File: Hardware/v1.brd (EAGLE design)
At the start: 77.5 x 32.6 mm, 23 parts, among them CN1 629105150521, CN2 TSW-120-08-L-S-RA, CN3 CONN_TE_DB9, CN4 CONN_TE_DB-HD15, IC1 ADUM3160BRWZ, IC3 IC_MAX3313, U1 TUSB2036VF

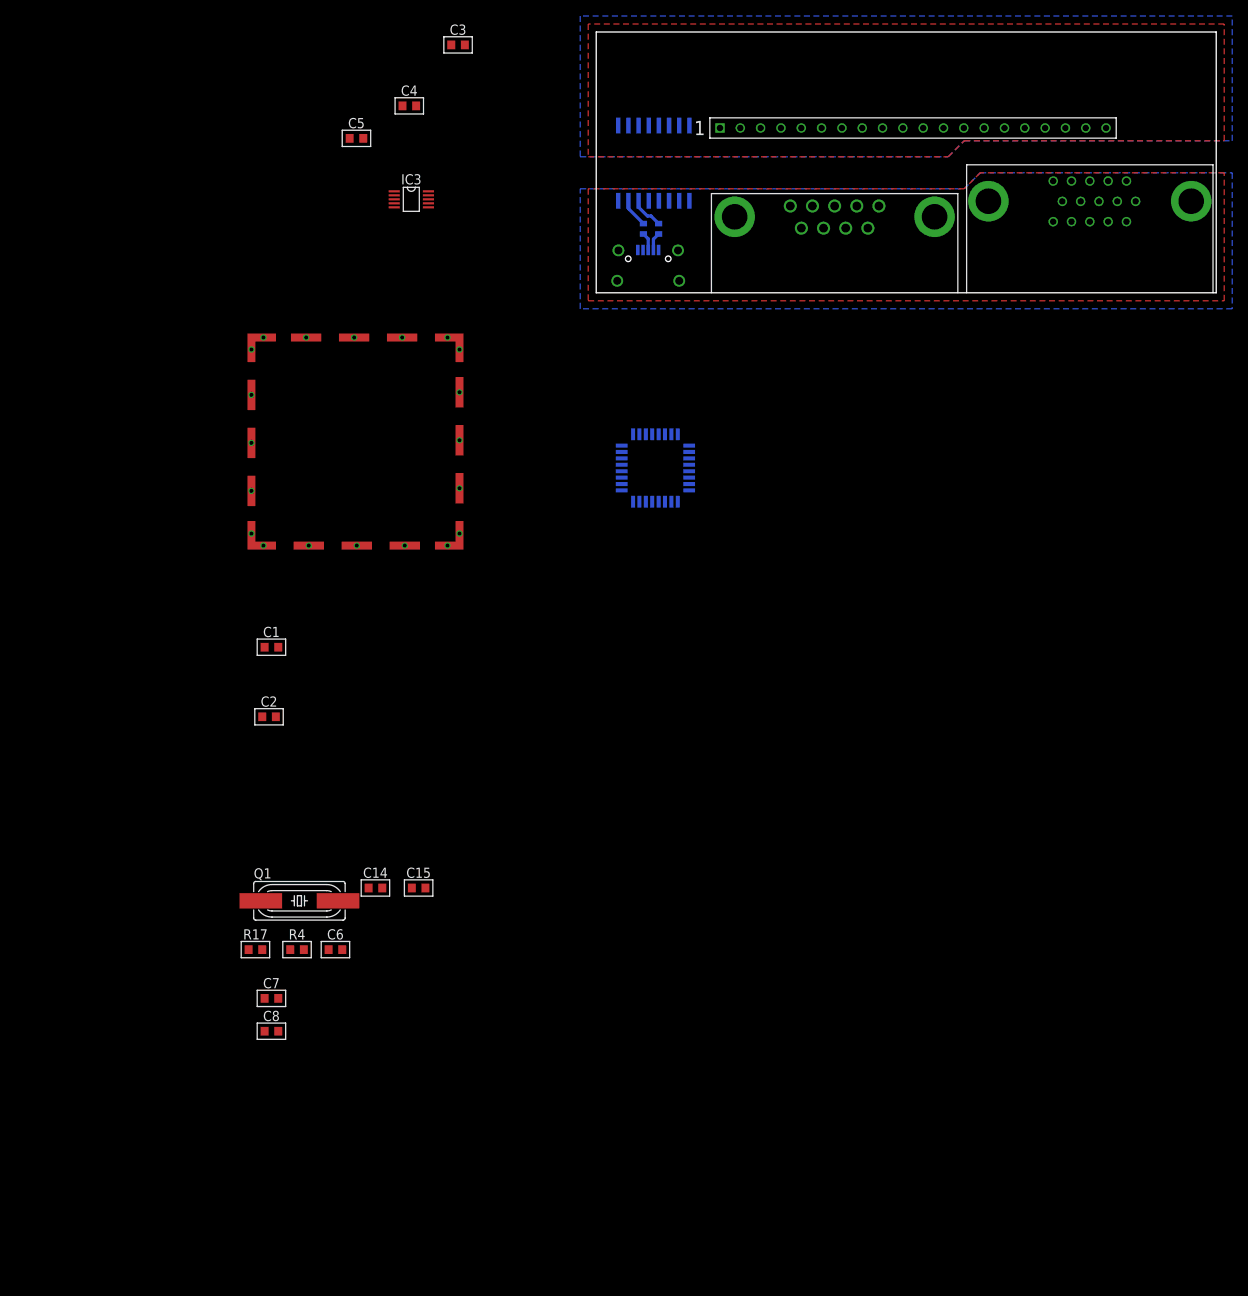
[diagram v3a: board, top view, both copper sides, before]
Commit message: finished input side of usb isolator
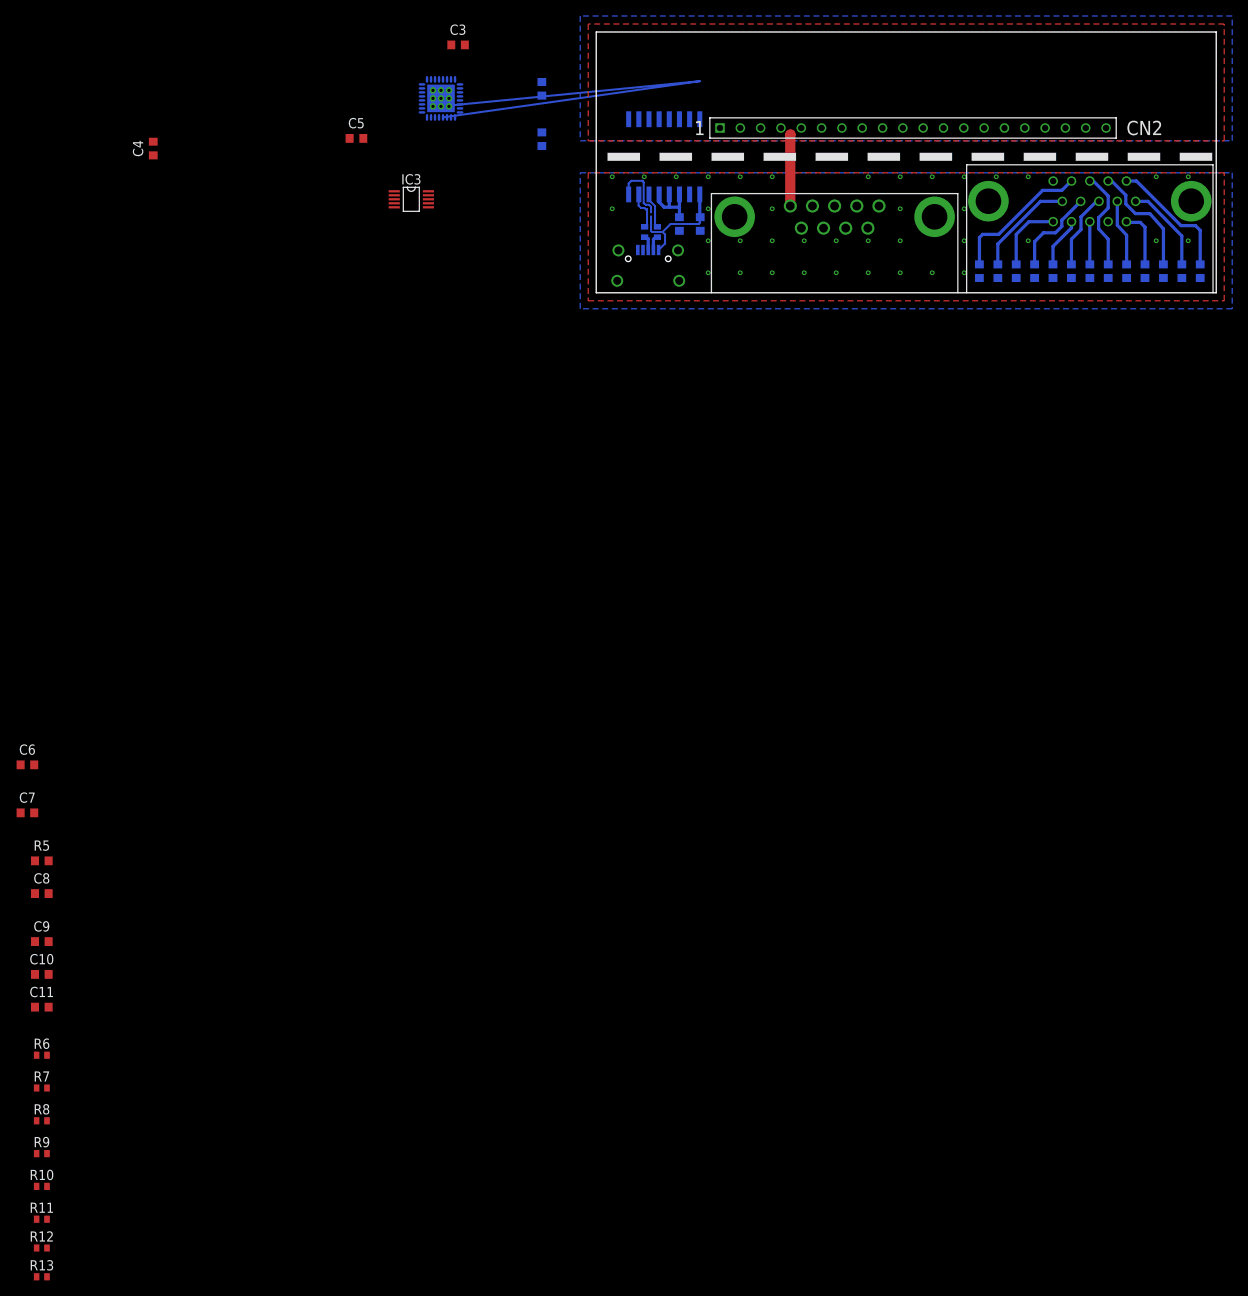
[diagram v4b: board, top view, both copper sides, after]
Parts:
- removed CAN1: CAN_LAIRD-BMI-S-203-F, m0wut:CAN_LAIRD_BMS-S-203-F
- removed Q1: (no value), adafruit:HC49UP
- removed R17: 1k5, rcl:R0603
- removed U1: TUSB2036VF, Texas Instruments_By_element14_Batch_1:QFP80P900X900X145-32N
- added C10, C11: 100nF, rcl:C0603
- added C12, C13, C16, C17, C18, C19, C20, C21, C22, C23, C24: 1nF, rcl:C0603
- added C9: 1uF, rcl:C0603
- added D1: D_ST_USBULC6, m0wut:UQFN6
- added IC2: TUSB2046BIRHBT, texas:RHB_S-PQFP-N32
- added R10, R11, R12, R13, R6, R7, R8, R9: 24, rcl:R0402
- added R3: 24, rcl:R0603
- added R5: 15k, rcl:R0603
- C14, C15: value 22pF -> 1nF
- CN3: value CONN_TE_DB9 -> 1734354-1
- CN4: value CONN_TE_DB-HD15 -> 1-1734530-1
- R4: value 15k -> 24
- moved C14 119.7 mm to (64.0, 2.70), flipped to the bottom, turned to 270 degrees
- moved R4 111.9 mm to (-6.80, 25.5), flipped to the bottom, turned to 90 degrees
- moved C15 104.2 mm to (47.9, 2.70), flipped to the bottom, turned to 270 degrees
- moved C2 80.2 mm to (10.4, 8.60), flipped to the bottom, turned to 270 degrees
- moved C1 75.3 mm to (13.0, 8.60), flipped to the bottom, turned to 270 degrees
- moved C6 44.9 mm to (-71.1, -59.0)
- moved C7 38.3 mm to (-71.1, -65.0)
- moved C8 33.5 mm to (-69.3, -75.1)
- moved C4 32.4 mm to (-55.4, 18.0), turned to 90 degrees
- moved IC1 1.53 mm to (8.50, 17.0)
- moved R1 0.43 mm to (6.05, 7.60)
- moved R2 0.43 mm to (7.65, 7.60)
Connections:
- removed net DP0PUR: U1.27
- removed net XTAL1: C14.1, Q1.1, U1.30
- removed net XTAL2: R17.2, U1.29
- new net 6MHZ_HUB: IC2.30
- new net D+: D1.1, D1.6, IC1.7, R1.2
- new net D-: D1.3, D1.4, IC1.6, R2.2
- new net DM4: R7.2
- new net DP4: R6.2
- new net N$12: IC2.11, R8.2
- new net N$13: IC2.12, R9.2
- new net N$14: IC2.15, R10.2
- new net N$15: IC2.16, R11.2
- new net N$16: IC2.20, R12.1
- new net N$17: IC2.19, R13.1
- new net N$18: C23.1, CN4.14
- new net N$19: CN4.12
- new net N$20: CN4.5
- new net N$21: C24.1, CN4.15
- new net N$22: C22.1, CN4.13
- new net N$23: C21.1, CN4.11
- new net N$24: C20.1, CN4.10
- new net N$25: C19.1, CN4.9
- new net N$26: C18.1, CN4.8
- new net N$27: C17.1, CN4.7
- new net N$28: C16.1, CN4.6
- new net N$29: C15.1, CN4.4
- new net N$30: C14.1, CN4.3
- new net N$31: C13.1, CN4.2
- new net N$32: C12.1, CN4.1
- new net VCC: C1.1, CN1.1, D1.5, IC1.1
- net +3V3: now also C10.1, C11.1, C6.1, C9.1, IC2.25, IC2.26, IC2.3, R5.1; no longer C8.1, R4.1, U1.10, U1.14, U1.18, U1.24, U1.25, U1.26, U1.3, U1.8
- net AGND: now also C12.2, C13.2, C14.2, C15.2, C16.2, C17.2, C18.2, C19.2, C20.2, C21.2, C22.2, C23.2, C24.2, CN3.TAB, CN3.TAB1, CN4.16, CN4.17, D1.2
- net DM0: now also IC2.2, R3.2; no longer IC1.11, U1.2
- net DM1: now also R8.1; no longer U1.11
- net DM2: now also R10.1; no longer U1.15
- net DM3: now also R13.2; no longer U1.19
- net DP0: now also IC2.1, R4.2; no longer IC1.10, U1.1
- net DP1: now also R9.1; no longer U1.12
- net DP2: now also R11.1; no longer U1.16
- net DP3: now also R12.2; no longer U1.20
- net GND: now also C10.2, C11.2, C6.2, C9.2, CN3.5, IC2.27, IC2.28, IC2.31, IC2.6, IC2.7, IC2.8, IC2.EXP, IC2.EXP@1, IC2.EXP@2, IC2.EXP@3, IC2.EXP@4, IC2.EXP@5, IC2.EXP@6, IC2.EXP@7, IC2.EXP@8, IC2.EXP@9; no longer C14.2, C15.2, C6.1, CAN1.P$1, CAN1.P$10, CAN1.P$11, CAN1.P$12, CAN1.P$13, CAN1.P$14, CAN1.P$15, CAN1.P$16, CAN1.P$17, CAN1.P$18, CAN1.P$19, CAN1.P$2, CAN1.P$20, CAN1.P$21, CAN1.P$22, CAN1.P$23, CAN1.P$24, CAN1.P$25, CAN1.P$26, CAN1.P$27, CAN1.P$28, CAN1.P$29, CAN1.P$3, CAN1.P$30, CAN1.P$31, CAN1.P$32, CAN1.P$33, CAN1.P$34, CAN1.P$35, CAN1.P$36, CAN1.P$37, CAN1.P$38, CAN1.P$39, CAN1.P$4, CAN1.P$40, CAN1.P$5, CAN1.P$6, CAN1.P$7, CAN1.P$8, CAN1.P$9, U1.21, U1.22, U1.23, U1.28, U1.31, U1.6, U1.7
- net N$10: now also IC1.11, R3.1; no longer C6.2, R4.2, U1.4
- net N$11: now also IC1.10, R4.1; no longer C15.1, Q1.2, R17.1
- net N$3: now also C8.1, IC2.4, R5.2; no longer IC1.6, R2.2
- net N$4: now also IC2.24, R6.1; no longer IC1.7, R1.2
- net N$5: now also IC2.23, R7.1; no longer C1.1, CN1.1, IC1.1
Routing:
- net GND: track 0.00 -> 73.9 mm
- net N$29: track 0.00 -> 17.8 mm
- net N$32: track 0.00 -> 16.0 mm
- net VCC: track 0.00 -> 14.5 mm
- net N$31: track 0.00 -> 14.5 mm
- net N$24: track 0.00 -> 12.8 mm
- net N$30: track 0.00 -> 12.6 mm
- net N$28: track 0.00 -> 11.1 mm
- net N$25: track 0.00 -> 11.1 mm
- net N$26: track 0.00 -> 9.49 mm
- net N$21: track 0.00 -> 9.03 mm
- net N$27: track 0.00 -> 8.33 mm
- net N$9: track 0.00 -> 8.29 mm
- net AGND: track 0.00 -> 7.65 mm, vias 0 -> 39
- net N$23: track 0.00 -> 7.26 mm
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
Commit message: most of usb hub implemented
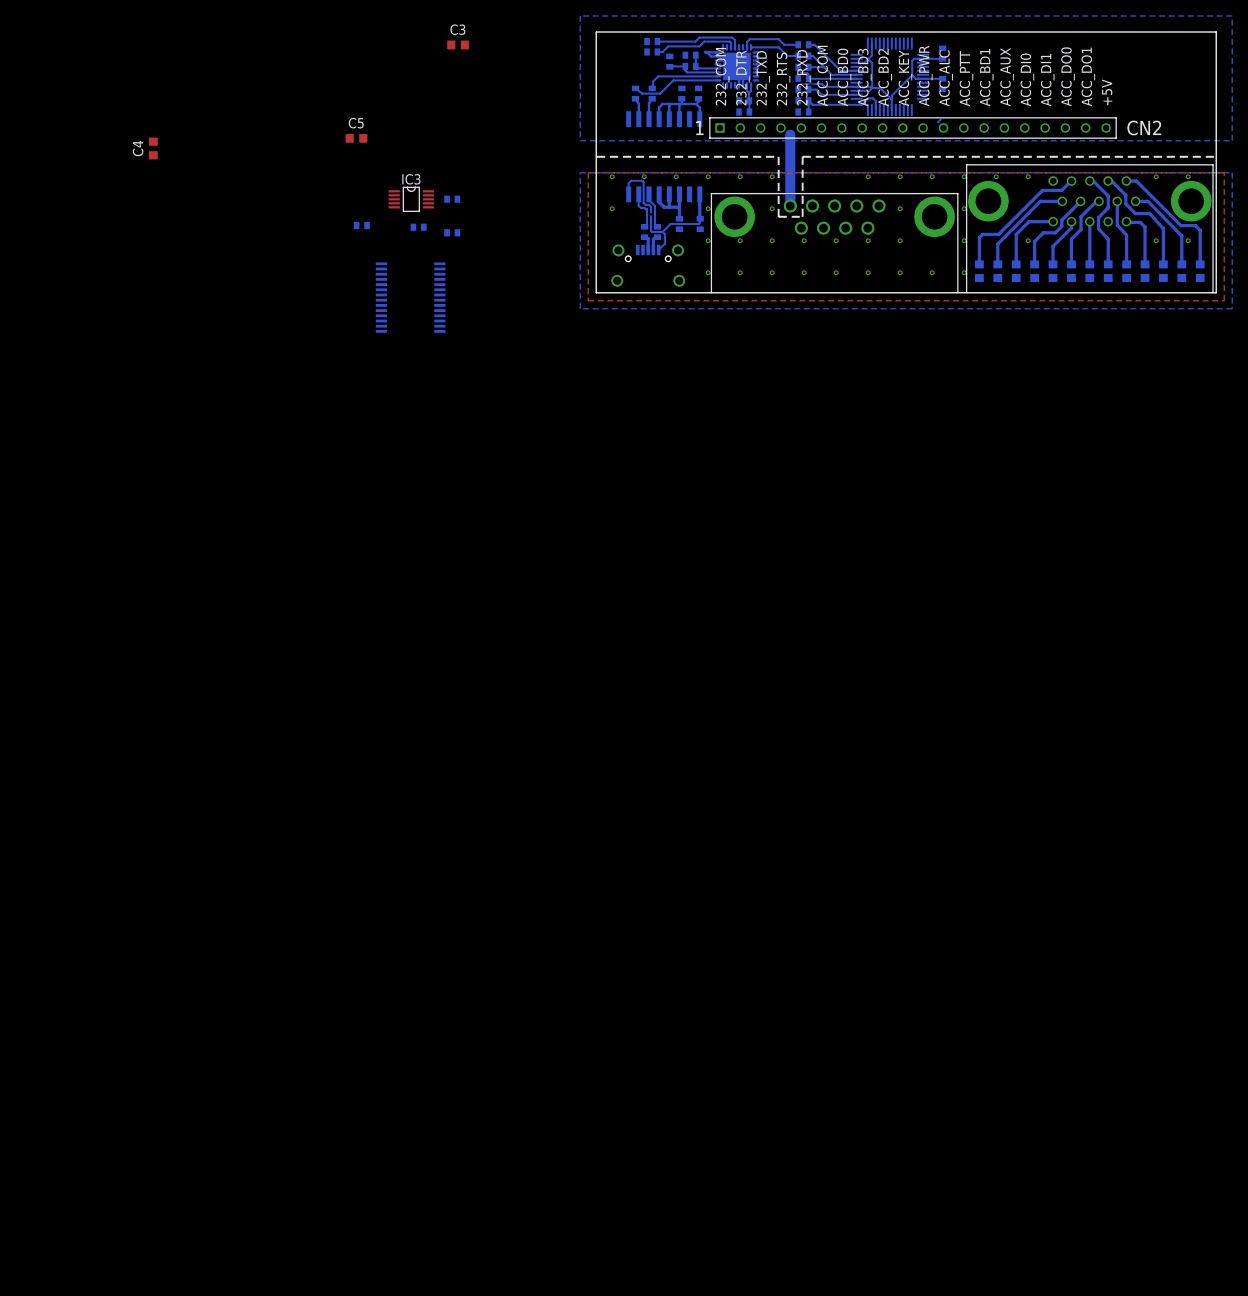
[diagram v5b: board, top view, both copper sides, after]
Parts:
- added C25, C27, C28: 100nF, rcl:C0402
- added C26: 33nF, rcl:C0402
- added IC4: FT2232D, ftdichip-3:QFP48-7X7
- added IC6: PCM2903C, texas:SSOP28DB
- added R14: 1k5, rcl:R0402
- added R15: 470, rcl:R0402
- added R16: 10k, rcl:R0402
- C1, C10, C11, C2, C6, C7, C8, C9: device rcl:C0603 -> rcl:C0402
- R3, R4, R5: device rcl:R0603 -> rcl:R0402
- moved R11 173.8 mm to (25.9, 29.6), flipped to the bottom
- moved R10 171.5 mm to (25.9, 31.0), flipped to the bottom
- moved R9 158.6 mm to (7.00, 31.4), flipped to the bottom, turned to 180 degrees
- moved R8 153.9 mm to (7.00, 30.1), flipped to the bottom, turned to 180 degrees
- moved R13 144.1 mm to (-18.0, 11.7), flipped to the bottom, turned to 180 degrees
- moved C11 141.9 mm to (9.20, 28.9), flipped to the bottom, turned to 90 degrees
- moved C10 140.1 mm to (18.5, 24.0), flipped to the bottom
- moved R12 136.9 mm to (-18.0, 7.50), flipped to the bottom, turned to 180 degrees
- moved C9 135.9 mm to (18.5, 22.6), flipped to the bottom
- moved C8 132.5 mm to (11.8, 29.7), flipped to the bottom
- moved R5 128.2 mm to (11.8, 28.3), flipped to the bottom, turned to 180 degrees
- moved C7 121.5 mm to (10.7, 24.9), flipped to the bottom, turned to 90 degrees
- moved C6 118.7 mm to (12.8, 24.9), flipped to the bottom, turned to 90 degrees
- moved R7 115.0 mm to (-29.3, 8.40), flipped to the bottom, turned to 180 degrees
- moved R6 113.7 mm to (-22.2, 8.20), flipped to the bottom, turned to 180 degrees
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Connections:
- new net 6MHZ_FT: IC4.43
- new net AGNDC: IC6.11
- new net AGNDP: IC6.18
- new net AGNDX: IC6.22
- new net CAT_232_TO_PIC: IC4.24
- new net CAT_PIC_TO_232: IC4.23
- new net DGND: IC6.26
- new net DGNDU: IC6.4
- new net N$33: C27.1, IC4.46, R15.1
- new net N$37: IC4.2, R16.2
- new net VBUS: IC6.3
- new net VCCCI: IC6.10
- new net VCCP2I: IC6.19
- new net VCCXI: IC6.23
- new net VCOM: IC6.14
- new net VDD: C26.1, IC4.6, R14.1
- new net VDDI: IC6.27
- new net WK_232_TO_PIC: IC4.40
- new net WK_PIC_TO_232: IC4.39
- net +5V: now also C25.1, C28.1, IC4.10, IC4.14, IC4.26, IC4.3, IC4.31, IC4.4, IC4.42, R15.2, R16.1
- net DM2: now also IC4.8
- net DM4: now also IC6.2
- net DP2: now also IC4.7, R14.2
- net DP4: now also IC6.1
- net GND: now also C25.2, C26.2, C27.2, C28.2, IC4.18, IC4.25, IC4.34, IC4.45, IC4.47, IC4.9; no longer IC2.EXP@1, IC2.EXP@2, IC2.EXP@3, IC2.EXP@4, IC2.EXP@5, IC2.EXP@6, IC2.EXP@7, IC2.EXP@8, IC2.EXP@9
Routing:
- net GND: track 73.9 -> 25.2 mm
- net +5V: track 0.00 -> 39.2 mm
- net +3V3: track 0.00 -> 24.8 mm
- net N$33: track 0.00 -> 11.6 mm
- net DP0: track 0.00 -> 11.2 mm
- net N$13: track 0.00 -> 10.9 mm
- net N$12: track 0.00 -> 10.4 mm
- net DM0: track 0.00 -> 9.26 mm
- net DP2: track 0.00 -> 8.92 mm
- net VDD: track 0.00 -> 8.43 mm
- net N$14: track 0.00 -> 7.51 mm
- net DM2: track 0.00 -> 7.35 mm
- net N$15: track 0.00 -> 6.35 mm
- net N$37: track 0.00 -> 6.27 mm
- net N$3: track 0.00 -> 4.28 mm
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- removed copper zone on layer 1, net GND
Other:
- board text added: "+5V"
- board text added: "232_COM"
- board text added: "232_DTR"
- board text added: "232_RTS"
- board text added: "232_RXD"
- board text added: "232_TXD"
- board text added: "ACC_ALC"
- board text added: "ACC_AUX"
- board text added: "ACC_BD0"
- board text added: "ACC_BD1"
- board text added: "ACC_BD2"
- board text added: "ACC_BD3"
- board text added: "ACC_COM"
- board text added: "ACC_DI0"
- board text added: "ACC_DI1"
- board text added: "ACC_DO0"
- board text added: "ACC_DO1"
- board text added: "ACC_KEY"
- board text added: "ACC_PTT"
- board text added: "ACC_PWR"
